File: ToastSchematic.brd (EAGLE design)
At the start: 90 x 75 mm, 84 parts, among them Q1 DMN63D8LDW, Q2 DMN63D8LDW, Q3 DMN63D8LDW, Q4 DMN63D8LDW, T1 BPX81, T2 BPX81, T3 BPX81, T4 BPX81, T5 BPX81, T6 BPX81, U3 DRV8839_DSS_12, U4 DRV8839_DSS_12

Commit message: Minor Fixes
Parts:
- removed C_BUZ: 100nF, rcl:C0603K
- added D1: (no value), adafruit:SOD-323F
- added LED7: (no value), led:LED5MM
- added R1: (no value), rcl:R0603
- moved U$8 32.2 mm to (55.2, 16.6)
- moved C_DISP 6.03 mm to (38.3, 37.8), turned to 270 degrees
- moved Q4 0.24 mm to (58.1, 61.5), turned to 90 degrees
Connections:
- removed net N$13 (its old number): Q4.4, SPK1.+
- removed net N$16 (its old number): LED1.K, Q1.4
- removed net N$22: LED2.K, Q1.1
- removed net N$24: LED4.K, Q2.1
- removed net N$25: LED5.K, Q3.4
- removed net N$26: LED6.K, Q3.1
- new net DISP_CE: U$6.7
- new net N$11: LED2.K, Q1.6
- new net N$12: LED3.K, Q2.3
- new net N$15: LED6.K, Q3.6
- new net N$18: LED4.K, Q2.6
- new net N$20: LED5.K, Q3.3
- new net N$21: LED7.A, R1.2
- new net N$9: LED1.K, Q1.3
- net +3V3: now also D1.C; no longer C_BUZ.1
- net DGND: now also C_M.2, C_M2.2, Q1.1, Q1.4, Q2.1, Q2.4, Q3.1, Q3.4, Q4.4; no longer C15.2, C_BUZ.2, Q1.3, Q1.6, Q2.3, Q2.6, Q3.3, Q3.6, Q4.3, R23.2, U$6.7, U$8.1
- net GND: now also LED7.K, U$8.1
- net MGND: no longer C_M.2, C_M2.2
- net N$23: now also D1.A, Q4.3, SPK1.+; no longer LED3.K, Q2.4
- net V_BATT: now also R1.1
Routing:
- net DGND: track 75.7 -> 33.8 mm, vias 25 -> 10
- net +5V: track 123.0 -> 93.2 mm
- net MGND: track 20.9 -> 3.16 mm, vias 3 -> 0
- net N$25: track 12.9 -> 0.00 mm
- net N$23: track 11.5 -> 0.00 mm, vias 1 -> 0
- net N$24: track 10.8 -> 0.00 mm, vias 1 -> 0
- net N$16 (its old number): track 10.1 -> 0.00 mm
- net N$22: track 7.09 -> 0.00 mm
- net N$10: track 6.41 -> 0.00 mm
- net BUZZER: track 22.0 -> 15.8 mm
- net N$13 (its old number): track 5.28 -> 0.00 mm
- net N$16: track 4.80 -> 0.00 mm
- net IR_FL: track 14.9 -> 10.2 mm
- net N$14: track 3.26 -> 0.00 mm
- net +3V3: track 80.6 -> 77.3 mm
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
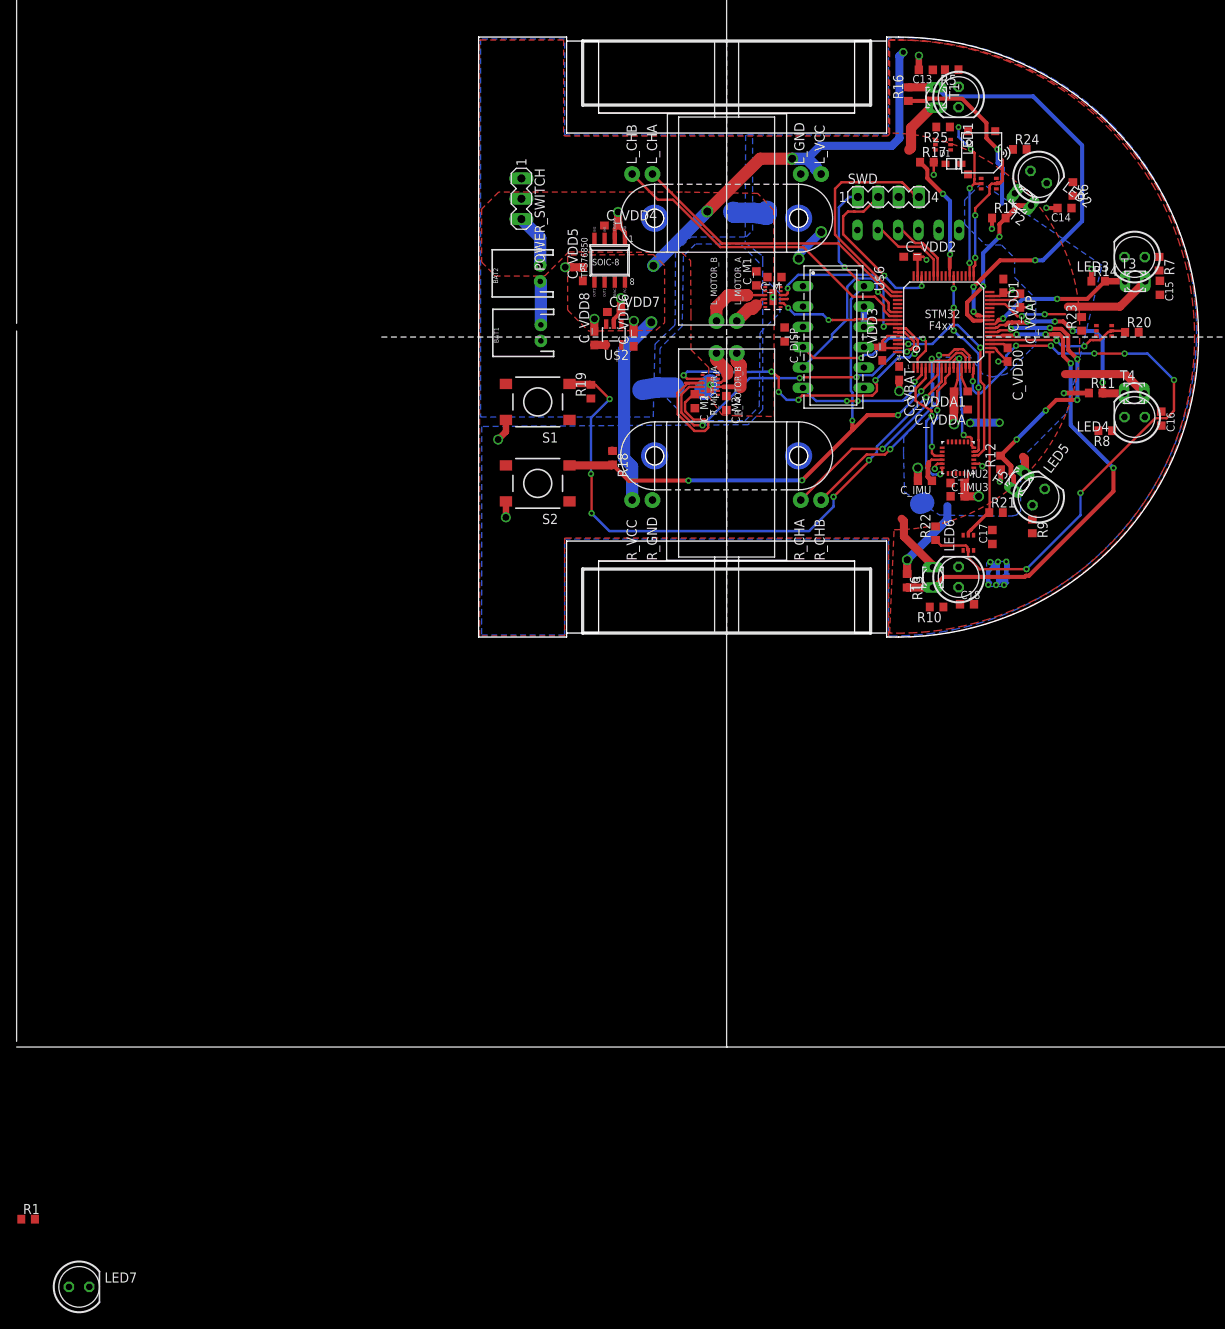
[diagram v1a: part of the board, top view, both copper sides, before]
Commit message: added routing and some mounting holes
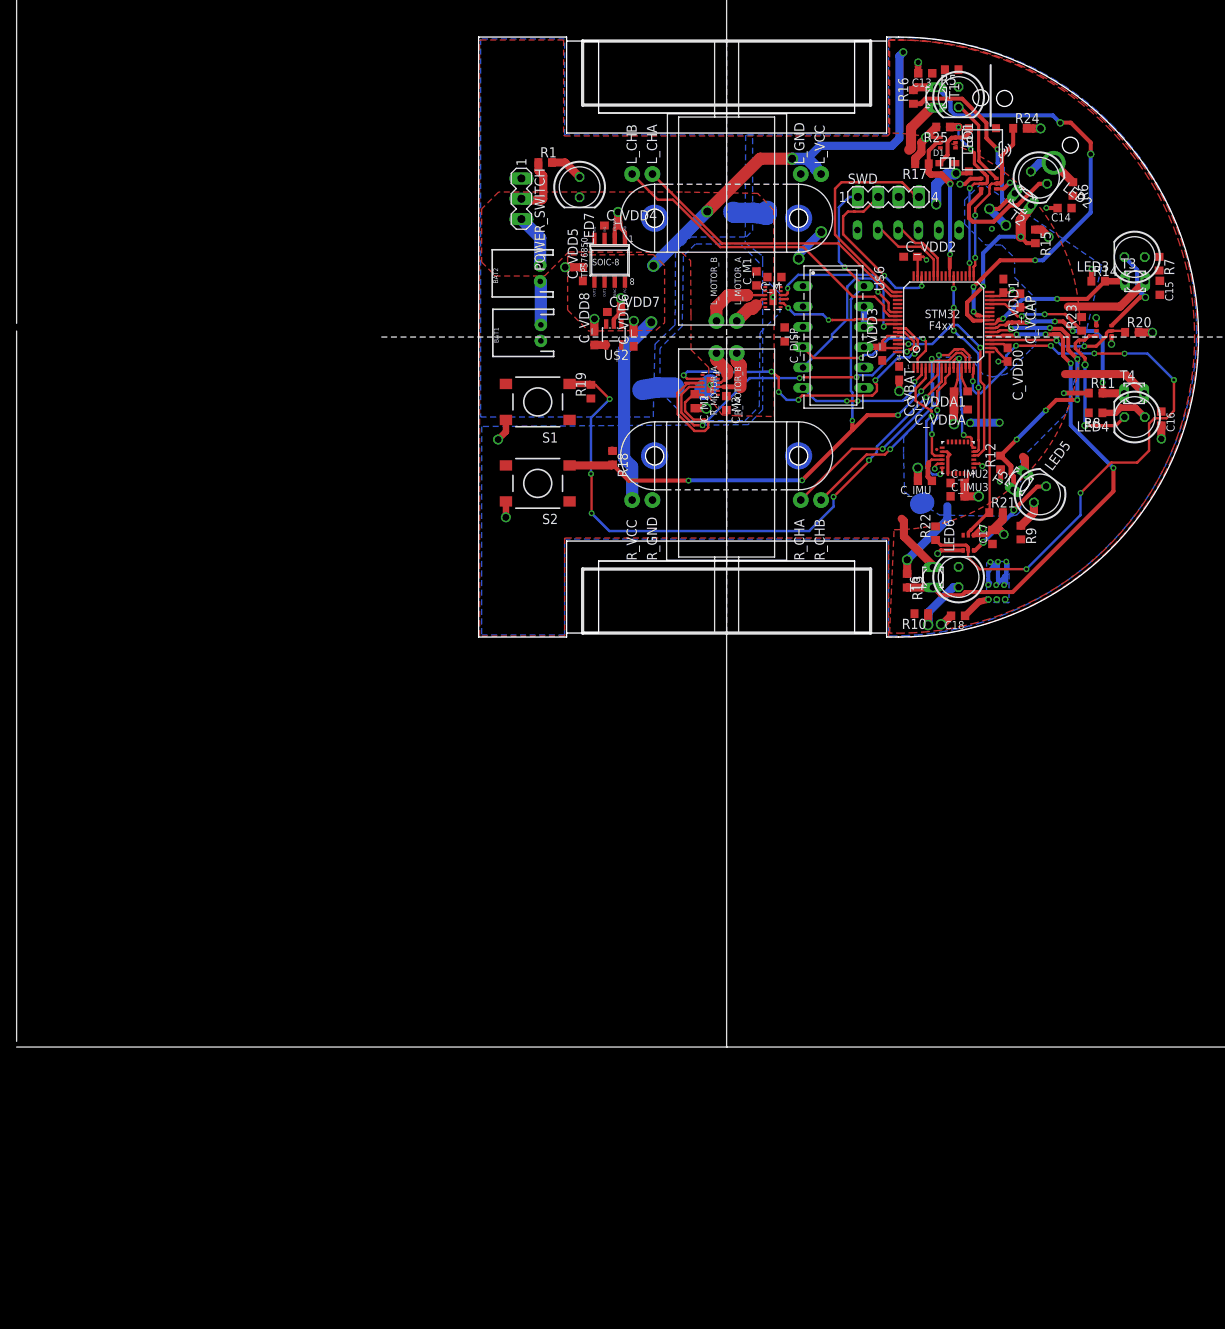
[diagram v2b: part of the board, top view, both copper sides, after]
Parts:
- moved LED7 151.0 mm to (12.6, 56.2), turned to 270 degrees
- moved R1 147.1 mm to (8.32, 59.3)
- moved R15 5.11 mm to (69.6, 50.1), turned to 270 degrees
- moved R24 2.64 mm to (67.7, 63.6)
- moved R8 2.54 mm to (77.1, 28.0)
- moved R10 2.08 mm to (55.3, 2.92)
- moved C18 1.82 mm to (59.9, 2.66), turned to 180 degrees
- moved R9 1.63 mm to (67.8, 13.1)
- moved D1 0.77 mm to (58.6, 59.2)
- moved R16 0.73 mm to (54.3, 67.5)
- moved Q4 0.66 mm to (58.7, 61.8)
- moved R17 0.65 mm to (55.4, 59.2), turned to 180 degrees
- moved C13 0.44 mm to (55.8, 70.5)
- moved SPK1 0.39 mm to (63.0, 60.9)
- moved LED5 0.38 mm to (70.2, 17.8)
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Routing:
- net DGND: track 33.8 -> 66.4 mm, vias 10 -> 22
- net N$18: track 0.00 -> 19.2 mm, vias 0 -> 2
- net +3V3: track 77.3 -> 95.0 mm, vias 4 -> 8
- net N$11: track 0.00 -> 16.2 mm
- net N$20: track 0.00 -> 12.5 mm, vias 0 -> 2
- net N$12: track 0.00 -> 11.9 mm, vias 0 -> 1
- net N$9: track 0.00 -> 11.0 mm
- net N$14: track 0.00 -> 8.11 mm, vias 0 -> 1
- net V_BATT: track 0.00 -> 7.71 mm
- net N$23: track 0.00 -> 6.83 mm
- net N$10: track 0.00 -> 6.72 mm, vias 0 -> 1
- net N$16: track 0.00 -> 6.06 mm
- net IR_DL: track 16.5 -> 21.1 mm
- net N$21: track 0.00 -> 4.20 mm
- net +5V: track 93.2 -> 96.9 mm, vias 11 -> 14
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
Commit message: fixed bottleneck and minor issues
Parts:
- moved LED7 8.21 mm to (4.88, 58.9), turned to 0 degrees
- moved R1 6.11 mm to (13.9, 56.9)
- moved POWER_SWITCH 4.73 mm to (10.1, 54.4)
- moved R17 2.44 mm to (54.1, 61.2), turned to 90 degrees
- moved C_M 0.86 mm to (37.6, 45.6), turned to 90 degrees
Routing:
- net GND: track 18.9 -> 60.8 mm, vias 5 -> 7
- net +3V3: track 95.0 -> 85.0 mm, vias 8 -> 4
- net N$21: track 4.20 -> 13.4 mm, vias 0 -> 1
- net BUZZER: track 19.4 -> 23.3 mm
- net V_BATT: track 7.71 -> 4.04 mm
- net AGND: track 59.3 -> 62.7 mm
- net SWCLK: track 28.3 -> 30.0 mm, vias 0 -> 1
- net DGND: track 66.4 -> 68.0 mm
- net CS: track 27.1 -> 28.2 mm, vias 2 -> 4
- net SCK: track 23.9 -> 24.6 mm, vias 4 -> 6
- net REC_FR: track 24.9 -> 25.6 mm, vias 4 -> 2
- net IR_DR: track 24.1 -> 24.3 mm, vias 0 -> 2
- net REC_DR: track 36.4 -> 36.3 mm, vias 6 -> 4
- net IR_FL: vias 2 -> 0
- net REC_R: vias 4 -> 2

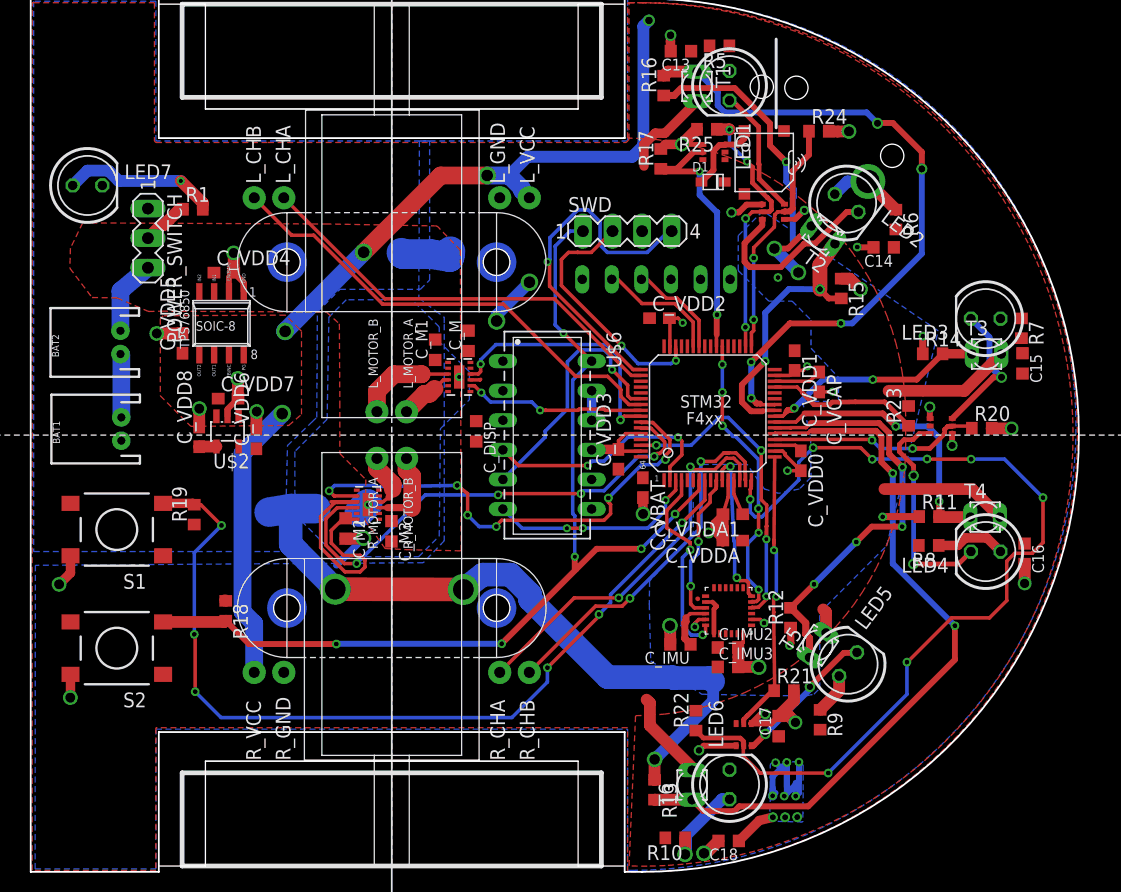
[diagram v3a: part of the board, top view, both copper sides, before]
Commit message: Added mounting holes for IR
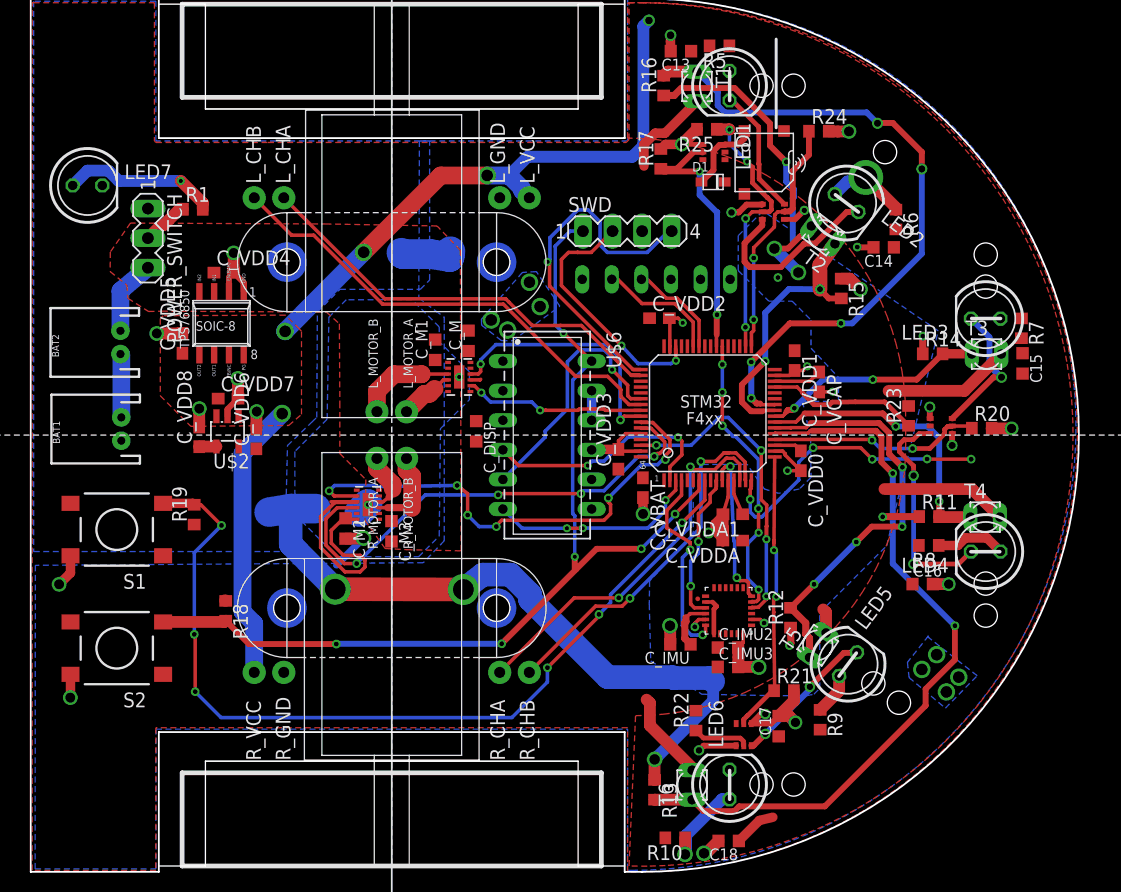
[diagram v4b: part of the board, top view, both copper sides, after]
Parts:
- moved C16 9.13 mm to (76.6, 24.7), turned to 0 degrees
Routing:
- net IR_R: track 81.0 -> 30.5 mm, vias 8 -> 5
- net +5V: track 96.9 -> 78.7 mm, vias 14 -> 9
- net +3V3: track 85.0 -> 80.5 mm, vias 4 -> 6
- net REC_R: track 62.8 -> 63.7 mm
- net L_ENC_A: track 37.0 -> 37.7 mm
- added copper zone on layer 16, net +3V3

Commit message: finished wiring everything
still need to add toast and butter pics on the back and smash and label
stuff
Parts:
- added LED8, LED9: (no value), led:CHIPLED_0603
- added R2, R3: (no value), resistor:R0603
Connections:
- new net LED1: R3.1, U$1.PC10
- new net LED2: R2.1, U$1.PC11
- new net N$22: LED8.A, R3.2
- new net N$25: LED9.A, R2.2
- net DGND: now also LED8.C, LED9.C
- net DISP_CE: now also U$1.PC12
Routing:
- net IR_R: track 30.5 -> 59.2 mm, vias 5 -> 6
- net DISP_CE: track 0.00 -> 18.7 mm, vias 0 -> 4
- net M_R_F: track 42.3 -> 60.9 mm, vias 4 -> 5
- net MGND: track 3.16 -> 20.9 mm, vias 0 -> 2
- net +3V3: track 80.5 -> 94.5 mm
- net LED1: track 0.00 -> 13.4 mm, vias 0 -> 1
- net DGND: track 67.7 -> 80.7 mm, vias 22 -> 27
- net N$22: track 0.00 -> 9.42 mm, vias 0 -> 1
- net N$25: track 0.00 -> 7.32 mm, vias 0 -> 1
- net N$15: track 0.00 -> 5.68 mm, vias 0 -> 1
- net LED2: track 0.00 -> 4.93 mm, vias 0 -> 1
- net N$8: track 0.00 -> 2.15 mm
- net IR_FL: track 13.1 -> 15.0 mm
- net N$13: track 0.00 -> 1.80 mm
- net REC_R: track 63.7 -> 64.9 mm, vias 2 -> 4
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
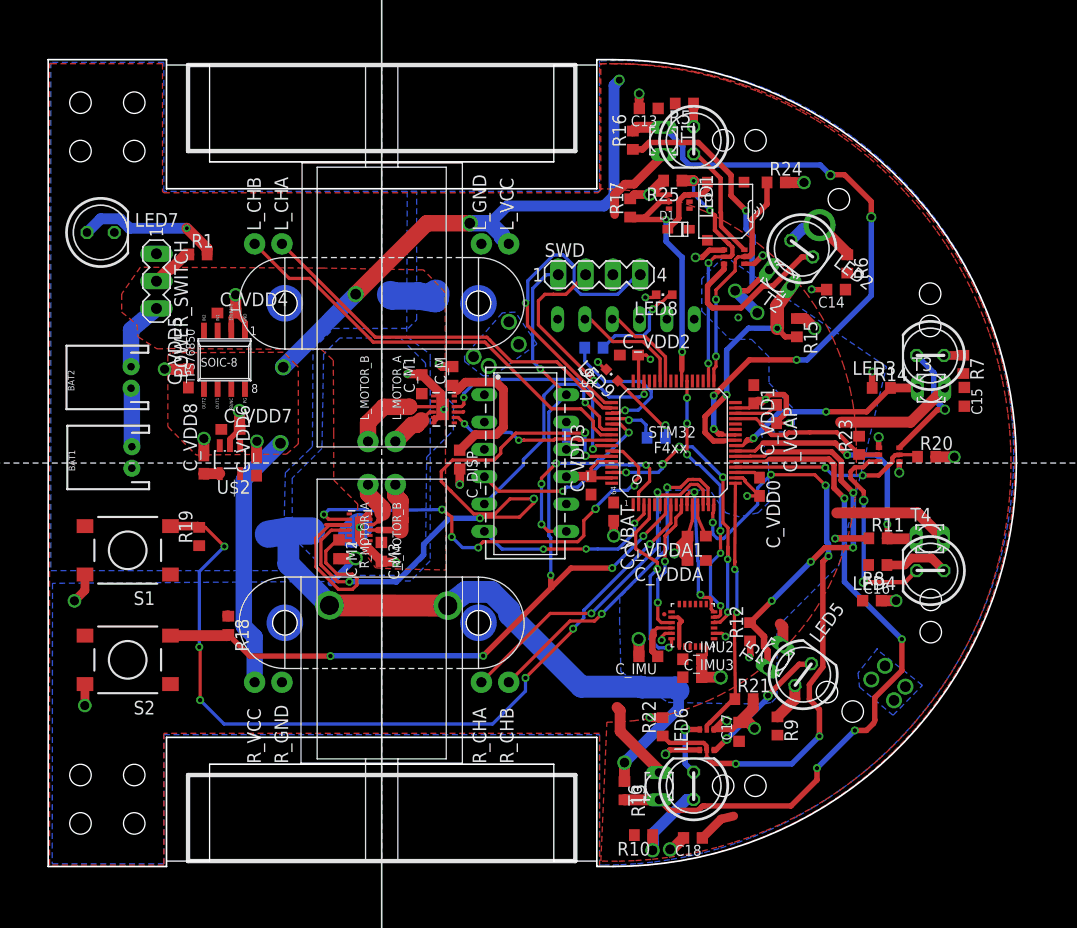
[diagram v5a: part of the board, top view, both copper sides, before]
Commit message: Added art to board
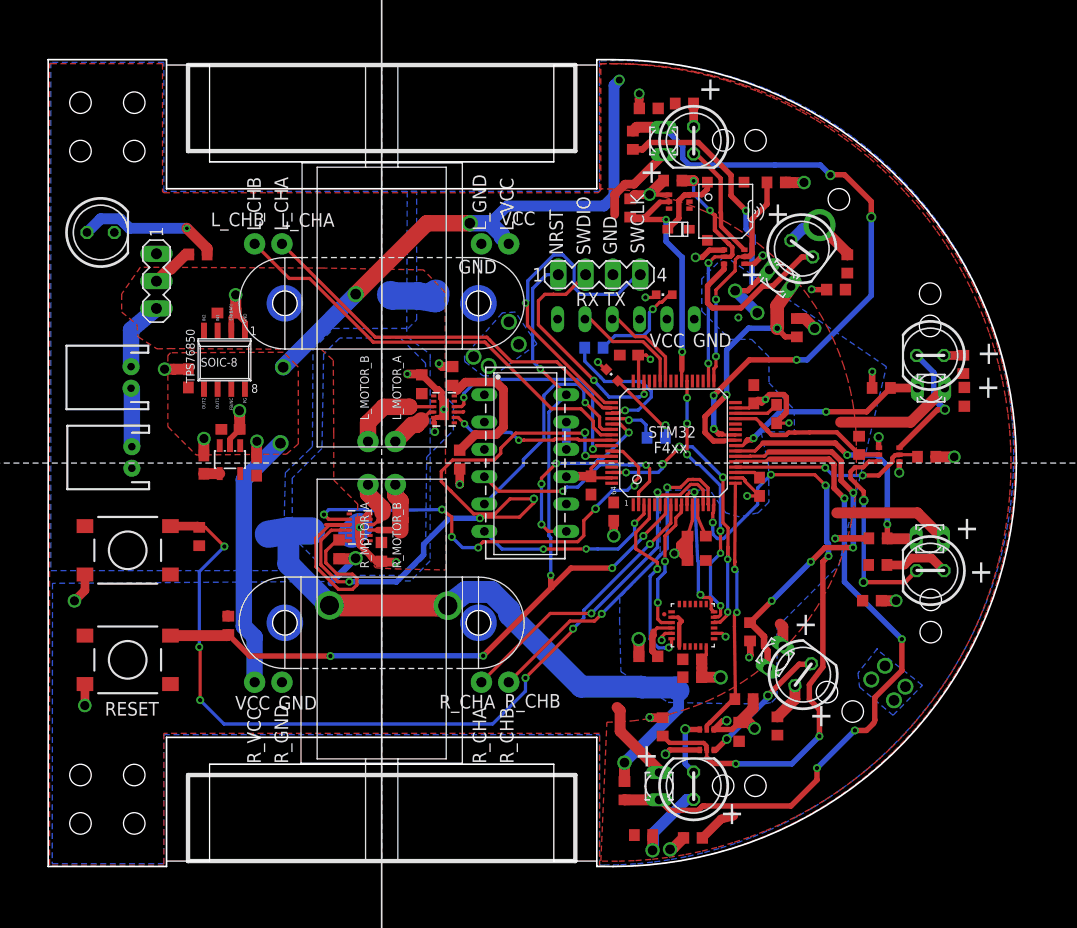
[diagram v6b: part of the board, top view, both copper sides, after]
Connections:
- net DGND: now also SV2.4
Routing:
- net MGND: track 20.9 -> 21.3 mm, vias 2 -> 3
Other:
- board text added: "+"
- board text added: "GND"
- board text added: "L_CHA"
- board text added: "L_CHB"
- board text added: "NRST"
- board text added: "RESET"
- board text added: "RX"
- board text added: "R_CHA"
- board text added: "R_CHB"
- board text added: "SWCLK"
- board text added: "SWDIO"
- board text added: "TX"
- board text added: "VCC"
